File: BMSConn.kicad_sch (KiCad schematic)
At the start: 6 parts, among them J2 CONN HEADER VERT 2POS 1.5MM, J3 CONN HEADER VERT 2POS 1.5MM, T1 PULSE XFMR 15UH 1 OHM FOR PLC

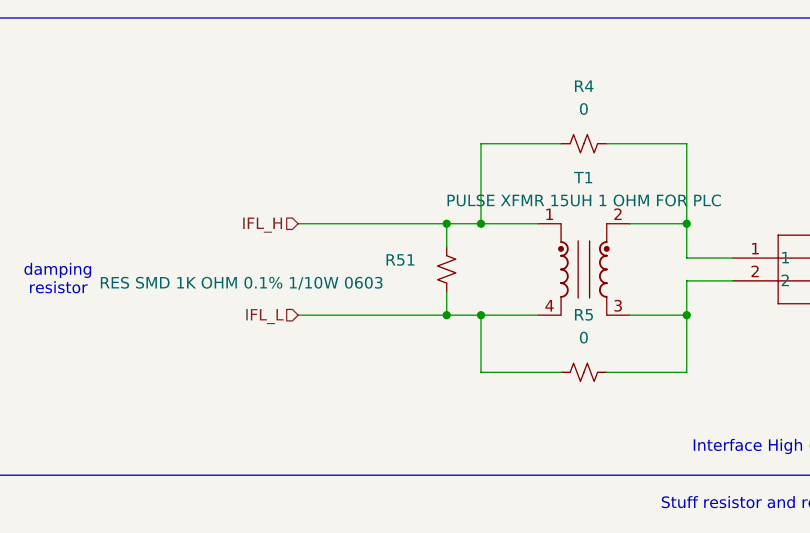
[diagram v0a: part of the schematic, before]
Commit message: initial component layout
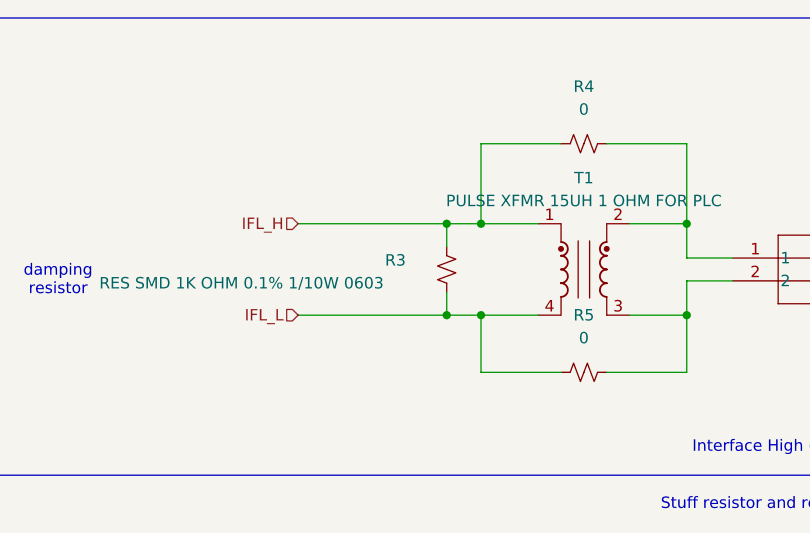
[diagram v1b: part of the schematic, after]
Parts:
- renumbered R51 to R3
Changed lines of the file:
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@@
 		(in_pos_files yes)
 		(dnp no)
-		(property "Reference" "R51"
+		(property "Reference" "R3"
 			(at 158.242 91.694 0)
 			(show_name no)
@@
 			(project "bms-afe"
 				(path "/226a23e7-09bb-40bc-b53a-ec42a6b7cc90/6d53ec20-967d-414a-950d-119f66d4f6c2"
-					(reference "R51")
+					(reference "R3")
 					(unit 1)
 				)

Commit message: fixed minor layout changes
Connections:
- net IFH_H renamed IFH_P
- net IFH_L renamed IFH_N
- net IFL_H renamed IFL_P
- net IFL_L renamed IFL_N
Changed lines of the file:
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@@
 		)
 	)
-	(hierarchical_label "IFL_L"
+	(hierarchical_label "IFL_N"
 		(shape input)
 		(at 148.59 97.79 180)
@@
 		)
 	)
-	(hierarchical_label "IFL_H"
+	(hierarchical_label "IFL_P"
 		(shape input)
 		(at 148.59 87.63 180)
@@
 		)
 	)
-	(hierarchical_label "IFH_L"
+	(hierarchical_label "IFH_N"
 		(shape input)
 		(at 83.82 92.71 0)
@@
 		)
 	)
-	(hierarchical_label "IFH_H"
+	(hierarchical_label "IFH_P"
 		(shape input)
 		(at 83.82 90.17 0)

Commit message: minor layout changes
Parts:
- added TP15, TP16, TP17, TP18: TestPoint, TestPoint:TestPoint_Pad_D1.0mm, symbol Connector:TestPoint
- R4, R5: value 0 -> RES 0 OHM JUMPER 1/10W 0603
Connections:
- net IFH_N: now also TP16.1
- net IFH_P: now also TP15.1
- net at J3.2, R5.2, T1.3: now also TP17.1
- net at J3.1, R4.2, T1.2: now also TP18.1
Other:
- moved on the sheet: J3
